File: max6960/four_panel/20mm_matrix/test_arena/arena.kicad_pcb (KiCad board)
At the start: 2 copper layers, 260 x 50 mm, 39 parts, among them M1 VAL**, M2 VAL**, M3 VAL**, M4 VAL**, M5 VAL**, M6 VAL**, P1 CONN15, P10 CONN_2X2, P11 CONN_2X2, P12 CONN_2X2, P13 CONN_2X2, P14 CONN_2X2, P15 CONN_2X2, P16 CONN_2X2, P17 CONN_2X2, P18 CONN_2X2, P19 CONN_2X2, P2 CONN15, P20 CONN_2X2, P21 CONN_2X2, P22 CONN_20X2, P23 CONN_30X2, P24 CONN_2, P25 CONN_2X2, P26 CONN_2, P3 CONN15, P4 CONN15, P5 CONN15, P6 CONN15, P7 CONN_2X2, P8 CONN_2X2, P9 CONN_2X2, U1 MAX7375

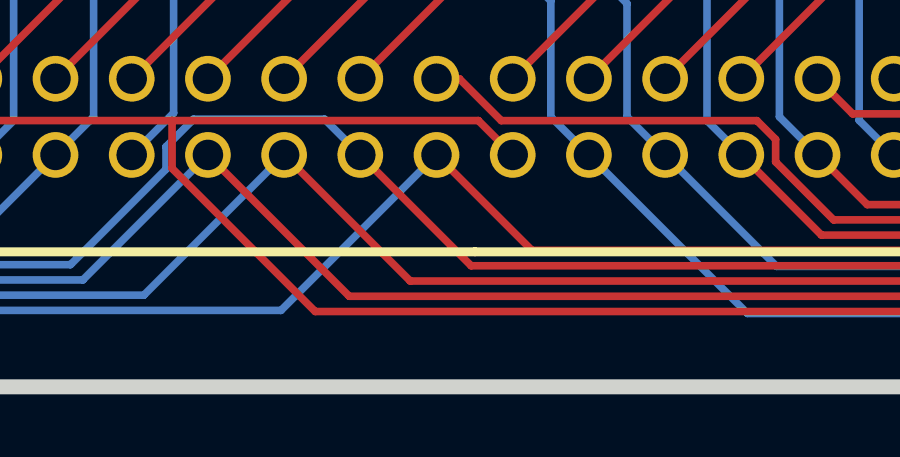
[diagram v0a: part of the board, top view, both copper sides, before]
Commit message: Fixed minor issues with test arenas and programmer pcbs.
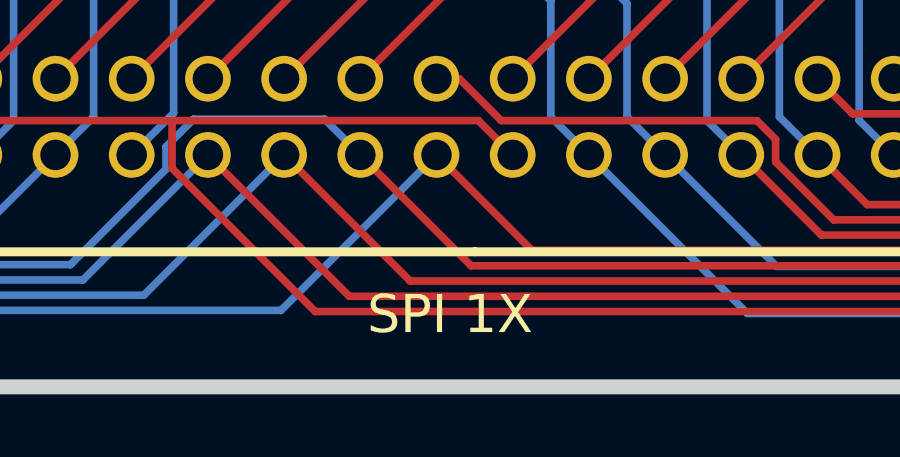
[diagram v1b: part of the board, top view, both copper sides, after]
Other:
- board text added: "SPI 1X"
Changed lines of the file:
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@@
     (links 181)
     (no_connects 0)
-    (area 39.749999 49.527499 311.349571 100.444321)
+    (area 39.749999 49.527499 310.381952 100.444321)
     (thickness 1.6)
-    (drawings 56)
+    (drawings 57)
     (tracks 912)
     (zones 0)
@@
     )
   )
+  (gr_text "SPI 1X" (at 116.1796 97.5868) (layer F.SilkS)
+    (effects (font (size 1.27 1.27) (thickness 0.254)))
+  )
   (gr_text INT (at 55.7276 65.3796 90) (layer F.SilkS)

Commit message: Added 3rd spi header to test arenas. Third header has 6 spi buses w/ 5 common cs lines.
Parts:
- added P27: CONN_5X2, PIN_ARRAY_5x2, F.Cu at (109.8, 77.0)
- added P28: CONN_5X2, PIN_ARRAY_5x2, F.Cu at (149.9, 77.0)
- added P29: CONN_5X2, PIN_ARRAY_5x2, F.Cu at (190.1, 77.0)
- added P30: CONN_5X2, PIN_ARRAY_5x2, F.Cu at (230.2, 77.0)
- added P31: CONN_5X2, PIN_ARRAY_5x2, F.Cu at (270.2, 77.0)
- added P32: CONN_20X2, PIN_ARRAY_SHRD_20X2, F.Cu at (174.0, 89.0)
- moved P23 13.2 mm to (250.0, 89.0)
- moved P22 7.28 mm to (110.0, 89.0)
- moved P10 4.00 mm to (222.7, 66.0)
- moved P11 4.00 mm to (262.8, 66.0)
- moved P12 4.00 mm to (109.8, 66.0)
- moved P13 4.00 mm to (149.9, 66.0)
- moved P14 4.00 mm to (190.1, 66.0)
- moved P15 4.00 mm to (230.2, 66.0)
- moved P16 4.00 mm to (270.2, 66.0)
- moved P17 4.00 mm to (117.3, 66.0)
- moved P18 4.00 mm to (157.4, 66.0)
- moved P19 4.00 mm to (197.6, 66.0)
- moved P20 4.00 mm to (237.7, 66.0)
- moved P21 4.00 mm to (277.8, 66.0)
- moved P7 4.00 mm to (102.3, 66.0)
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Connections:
- U1 pad 2: /INT_OSC -> /OSC_INT
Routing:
- net /CS5_0: track 192.1 -> 334.5 mm
- net /MISO_5: track 35.7 -> 152.8 mm, vias 1 -> 0
- net /MOSI_5: track 30.7 -> 139.3 mm
- net /CLK_5: track 26.0 -> 120.6 mm
- net /MOSI_4: track 19.8 -> 107.6 mm, vias 0 -> 1
- net /CLK_4: track 19.1 -> 103.6 mm, vias 0 -> 2
- net /CS2_0: track 193.4 -> 277.8 mm, vias 0 -> 2
- net /CS3_0: track 198.5 -> 278.7 mm, vias 0 -> 2
- net /CS4_0: track 220.5 -> 298.2 mm, vias 0 -> 2
- net /CS1_0: track 194.9 -> 270.0 mm, vias 0 -> 4
- net /CS3_3: track 146.4 -> 216.2 mm, vias 1 -> 3
- net /MISO_4: track 35.9 -> 103.3 mm, vias 0 -> 1
- net /CS5_2: track 204.9 -> 270.5 mm
- net /MISO_0: track 284.6 -> 340.1 mm, vias 1 -> 2
- net /MISO_3: track 23.2 -> 73.2 mm
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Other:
- board text added: "CS-COMMON"
- board text added: "SPI 1X, COMMON CS"
